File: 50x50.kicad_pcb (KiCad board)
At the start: 4 copper layers, 50 x 50 mm, 78 parts, among them J1 Conn_01x02, J2 Conn_01x02, J3 USB_C_Receptacle_USB2.0_14P, J4 Conn_01x03, J5 Conn_01x04, SW1 Reset, SW2 SW_SPST, U1 W25Q128JVPIQ TR, U2 RP2040, U4 Voltage Regulator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

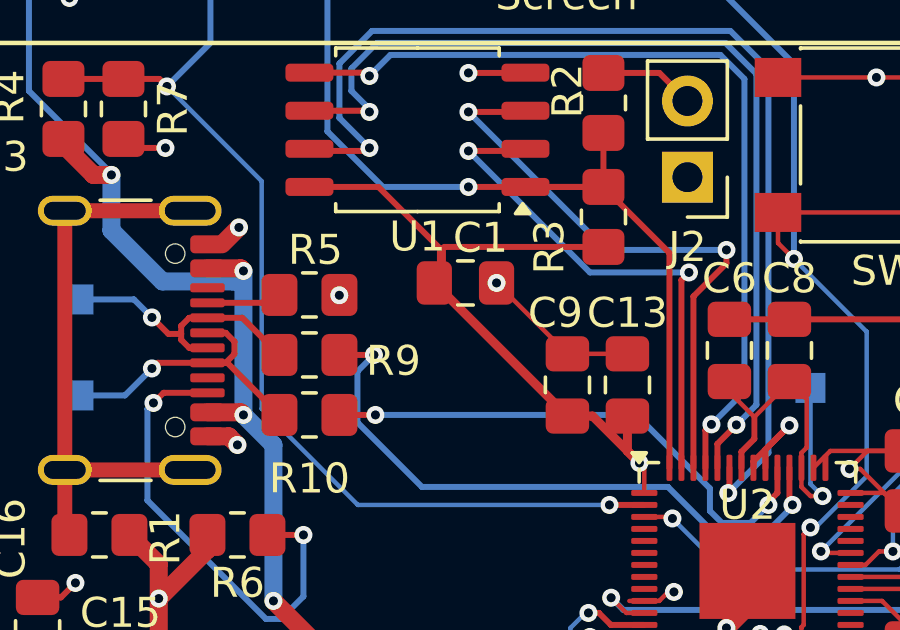
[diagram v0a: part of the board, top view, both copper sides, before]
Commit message: fix: moved all vias from under pads
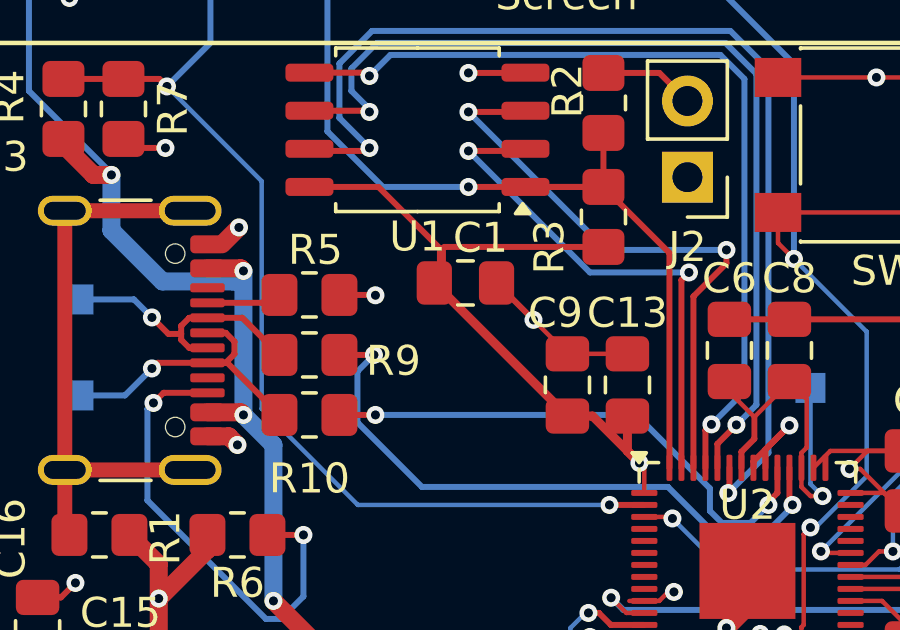
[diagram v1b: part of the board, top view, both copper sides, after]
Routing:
- net GND: track 86.7 -> 87.9 mm
